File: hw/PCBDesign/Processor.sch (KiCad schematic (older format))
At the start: 40 parts, among them J4 Conn_ARM_JTAG_SWD_10, Q2 MMBT3904, U11 74HC595, U13 STM32F446RETx, Y1 8MHz Crystal

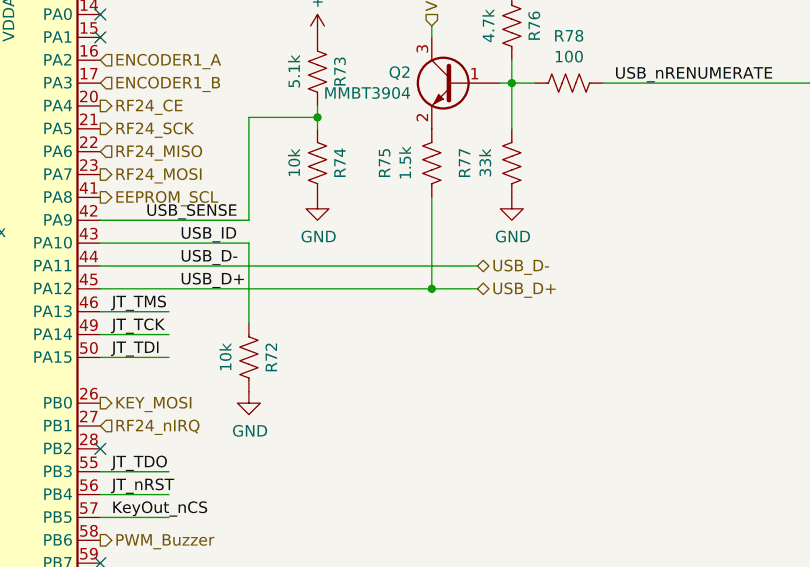
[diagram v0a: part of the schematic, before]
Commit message: Work further on v2.0 of controller pcb
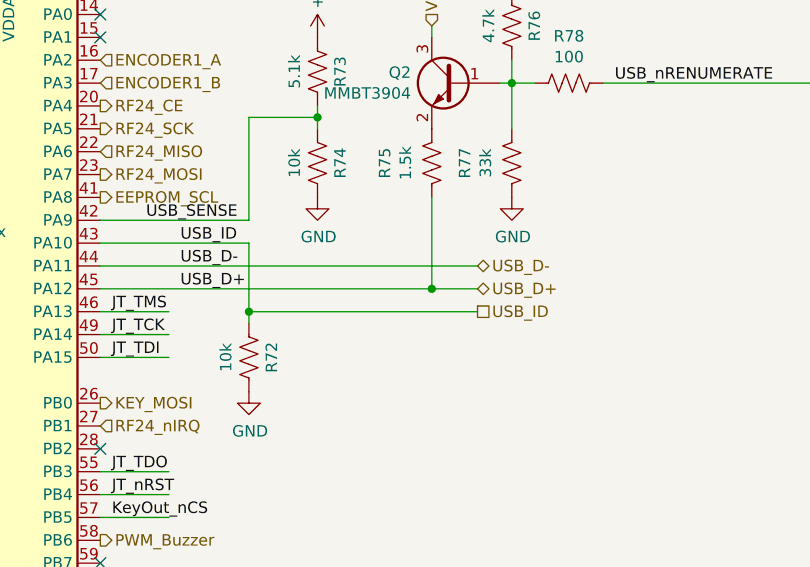
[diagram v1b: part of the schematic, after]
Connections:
- wire segments 99 -> 101
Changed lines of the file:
@@
 $EndComp
 Wire Wire Line
-	9450 2750 9450 2400
+	9450 2750 9450 2700
 Wire Wire Line
 	9450 2400 8800 2400
@@
 	-1   0    0    -1
 $EndComp
+Text HLabel 10450 2700 2    50   UnSpc ~ 0
+USB_ID
+Wire Wire Line
+	10450 2700 9450 2700
+Connection ~ 9450 2700
+Wire Wire Line
+	9450 2700 9450 2400
 $EndSCHEMATC

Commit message: Improve PCB design
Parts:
- removed C53, C54: 1.5pF, Capacitor_SMD:C_0402_1005Metric, symbol Device:C
- removed Y1: 8MHz Crystal, Crystal:Crystal_SMD_5032-2Pin_5.0x3.2mm, symbol Device:Crystal
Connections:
- wire segments 101 -> 91
- no-connect marks 10 -> 12
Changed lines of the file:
@@
 Wire Wire Line
 	4450 2400 3350 2400
-$Comp
-L Device:Crystal Y1
-U 1 1 604DCFCD
-P 6400 2500
-F 0 "Y1" V 6354 2631 50  0000 L CNN
-F 1 "8MHz Crystal" V 6445 2631 50  0000 L CNN
-F 2 "Crystal:Crystal_SMD_5032-2Pin_5.0x3.2mm" H 6400 2500 50  0001 C CNN
-F 3 "~" H 6400 2500 50  0001 C CNN
-F 4 "C115962" V 6400 2500 50  0001 C CNN "LCSC"
-	1    6400 2500
-	0    1    1    0
-$EndComp
-$Comp
-L Device:C C53
-U 1 1 604DDB41
-P 6150 2300
-F 0 "C53" V 6300 2300 50  0000 C CNN
-F 1 "1.5pF" V 5989 2300 50  0000 C CNN
-F 2 "Capacitor_SMD:C_0402_1005Metric" H 6188 2150 50  0001 C CNN
-F 3 "~" H 6150 2300 50  0001 C CNN
-F 4 "C1552" H 6150 2300 50  0001 C CNN "LCSC"
-	1    6150 2300
-	0    1    1    0
-$EndComp
-$Comp
-L Device:C C54
-U 1 1 604DE10D
-P 6150 2700
-F 0 "C54" V 6300 2700 50  0000 C CNN
-F 1 "1.5pF" V 5989 2700 50  0000 C CNN
-F 2 "Capacitor_SMD:C_0402_1005Metric" H 6188 2550 50  0001 C CNN
-F 3 "~" H 6150 2700 50  0001 C CNN
-F 4 "C1552" H 6150 2700 50  0001 C CNN "LCSC"
-	1    6150 2700
-	0    1    1    0
-$EndComp
-$Comp
-L power:GND #PWR0103
-U 1 1 604DE54A
-P 6000 2700
-F 0 "#PWR0103" H 6000 2450 50  0001 C CNN
-F 1 "GND" V 6005 2572 50  0000 R CNN
-F 2 "" H 6000 2700 50  0001 C CNN
-F 3 "" H 6000 2700 50  0001 C CNN
-	1    6000 2700
-	0    1    1    0
-$EndComp
-$Comp
-L power:GND #PWR0102
-U 1 1 604DED19
-P 6000 2300
-F 0 "#PWR0102" H 6000 2050 50  0001 C CNN
-F 1 "GND" V 6005 2172 50  0000 R CNN
-F 2 "" H 6000 2300 50  0001 C CNN
-F 3 "" H 6000 2300 50  0001 C CNN
-	1    6000 2300
-	0    1    1    0
-$EndComp
-Wire Wire Line
-	6300 2300 6400 2300
-Wire Wire Line
-	6400 2300 6400 2350
-Wire Wire Line
-	7400 2500 6850 2500
-Wire Wire Line
-	6850 2500 6850 2300
-Wire Wire Line
-	6850 2300 6400 2300
-Connection ~ 6400 2300
-Wire Wire Line
-	7400 2600 6850 2600
-Wire Wire Line
-	6300 2700 6400 2700
-Wire Wire Line
-	6400 2700 6400 2650
-Wire Wire Line
-	6400 2700 6850 2700
-Wire Wire Line
-	6850 2700 6850 2600
-Connection ~ 6400 2700
 Text HLabel 3350 1900 2    50   Output ~ 0
 RF24_VCC_EN
@@
 Wire Wire Line
 	9450 2700 9450 2400
+NoConn ~ 7400 2500
+NoConn ~ 7400 2600
 $EndSCHEMATC

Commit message: Add more of the I2C driver
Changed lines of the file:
@@
 Text HLabel 8800 1700 2    50   Input ~ 0
 ENCODER1_B
+Text HLabel 7400 3200 0    50   Input ~ 0
+ANALOG_IN_VPITCH
+Text HLabel 7400 3300 0    50   Input ~ 0
+ANALOG_IN_VROLL
 Text HLabel 7400 3100 0    50   Input ~ 0
-ANALOG_IN_VPITCH
+ANALOG_IN_VYAW
 Text HLabel 7400 3000 0    50   Input ~ 0
-ANALOG_IN_VROLL
-Text HLabel 7400 3300 0    50   Input ~ 0
-ANALOG_IN_VYAW
-Text HLabel 7400 3200 0    50   Input ~ 0
 ANALOG_IN_VTHROTTLE
 Wire Wire Line

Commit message: Finish first draft of v2.0 pcb
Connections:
- net labels removed: PWM_Buzzer
- wire segments 91 -> 93
- no-connect marks 12 -> 13
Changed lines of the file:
@@
 $Descr A3 16535 11693
 encoding utf-8
-Sheet 11 11
+Sheet 10 10
 Title ""
 Date ""
@@
 Text HLabel 7200 1400 0    50   Input ~ 0
 nRESET
-Text HLabel 8800 3700 2    50   Output ~ 0
-PWM_Buzzer
-Text HLabel 8800 3100 2    50   Output ~ 0
-KEY_MOSI
 Text HLabel 7400 4100 0    50   Input ~ 0
 KEY_MISO
@@
 Text HLabel 2550 2100 0    50   Output ~ 0
 KEY_SCK
-Text HLabel 2550 1900 0    50   Output ~ 0
-KEY_MOSI
 Text Label 1950 2400 0    50   ~ 0
 KeyOut_nCS
@@
 NoConn ~ 7400 2500
 NoConn ~ 7400 2600
+NoConn ~ 8800 3700
+Wire Wire Line
+	2550 1900 2000 1900
+Text Label 2050 1900 0    50   ~ 0
+KEY_MOSI
+Wire Wire Line
+	8800 3100 9250 3100
+Text Label 8850 3100 0    50   ~ 0
+KEY_MOSI
 $EndSCHEMATC
